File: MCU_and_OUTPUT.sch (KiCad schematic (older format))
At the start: 32 parts, among them P5 CONN_5, P6 CONN_01X04, Q2 BC817-40, Q3 BC817-40, Q4 BC807-40, Q5 IRF540, U2 STM32F030K6, U3 LM358

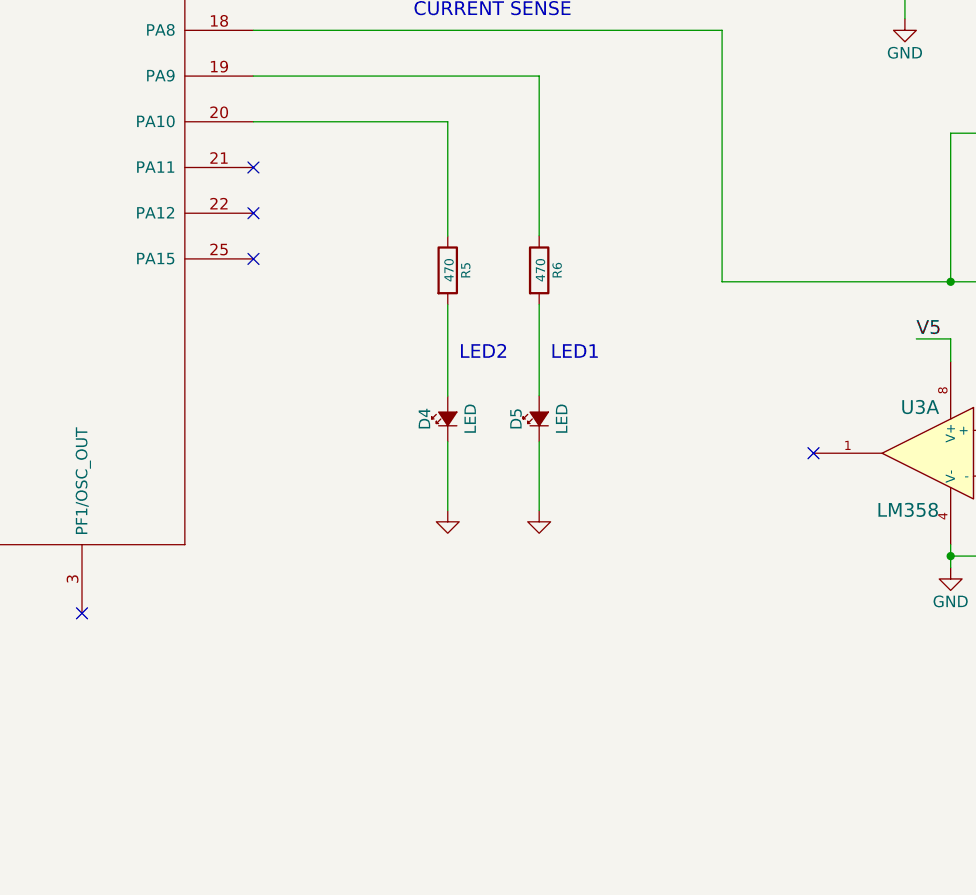
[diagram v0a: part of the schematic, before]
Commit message: agregue pulsador de arranque y buzzer
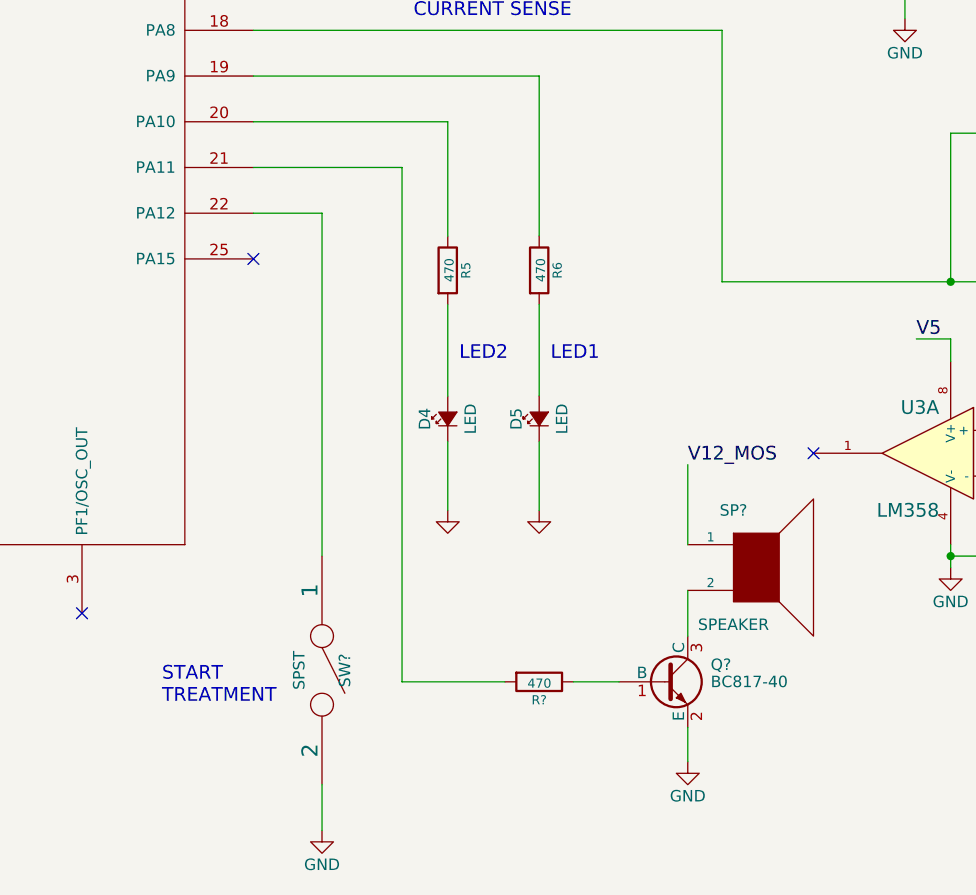
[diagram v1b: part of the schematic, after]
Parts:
- added Q?: BC817-40, MOSFET:BC817_SOT-23, symbol BC817-40
- added R?: 470, Resistors_SMD:R_0805_HandSoldering, symbol R
- added SP?: SPEAKER, symbol SPEAKER
- added SW?: SPST, symbol SPST
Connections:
- net GND: now also Q?.2 (E), SW?.2
- net V12_MOSFET: now also SP?.1
- net at U2.21 (PA11): now also R?.2
- net at U2.22 (PA12): now also SW?.1
- new net: Q?.1 (B), R?.1
- new net: Q?.3 (C), SP?.2
- no-connect marks 20 -> 18
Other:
- note added: "START\nTREATMENT"
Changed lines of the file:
@@
 	1    0    0    -1
 $EndComp
-NoConn ~ 4250 4800
 NoConn ~ 4250 5000
 NoConn ~ 1300 3200
@@
 $EndComp
 NoConn ~ 7550 6950
-NoConn ~ 4250 4600
 NoConn ~ 4250 2600
 Text HLabel 8300 800  2    60   Input ~ 0
@@
 Connection ~ 7300 6300
 NoConn ~ 6700 5850
+$Comp
+L GND #PWR?
+U 1 1 56FFF54C
+P 6150 7200
+F 0 "#PWR?" H 6150 6950 50  0001 C CNN
+F 1 "GND" H 6150 7050 50  0000 C CNN
+F 2 "" H 6150 7200 60  0000 C CNN
+F 3 "" H 6150 7200 60  0000 C CNN
+	1    6150 7200
+	1    0    0    -1
+$EndComp
+Text Label 6150 5900 0    60   ~ 0
+V12_MOS
+$Comp
+L BC817-40 Q?
+U 1 1 56FFF553
+P 6050 6850
+F 0 "Q?" H 6250 6925 50  0000 L CNN
+F 1 "BC817-40" H 6250 6850 50  0000 L CNN
+F 2 "MOSFET:BC817_SOT-23" H 6250 6775 50  0001 L CIN
+F 3 "" H 6050 6850 50  0000 L CNN
+	1    6050 6850
+	1    0    0    -1
+$EndComp
+Wire Wire Line
+	6150 6450 6150 6650
+Wire Wire Line
+	6150 7050 6150 7200
+Wire Wire Line
+	6150 5900 6150 6250
+$Comp
+L SPST SW?
+U 1 1 56FFFC2E
+P 4550 6800
+F 0 "SW?" H 4550 6900 50  0000 C CNN
+F 1 "SPST" H 4550 6700 50  0000 C CNN
+F 2 "" H 4550 6800 60  0000 C CNN
+F 3 "" H 4550 6800 60  0000 C CNN
+	1    4550 6800
+	0    1    1    0
+$EndComp
+$Comp
+L SPEAKER SP?
+U 1 1 56FFFCAD
+P 6450 6350
+F 0 "SP?" H 6350 6600 50  0000 C CNN
+F 1 "SPEAKER" H 6350 6100 50  0000 C CNN
+F 2 "" H 6450 6350 60  0000 C CNN
+F 3 "" H 6450 6350 60  0000 C CNN
+	1    6450 6350
+	1    0    0    -1
+$EndComp
+$Comp
+L GND #PWR?
+U 1 1 57000B38
+P 4550 7500
+F 0 "#PWR?" H 4550 7250 50  0001 C CNN
+F 1 "GND" H 4550 7350 50  0000 C CNN
+F 2 "" H 4550 7500 60  0000 C CNN
+F 3 "" H 4550 7500 60  0000 C CNN
+	1    4550 7500
+	1    0    0    -1
+$EndComp
+Wire Wire Line
+	4550 7300 4550 7500
+$Comp
+L R R?
+U 1 1 5700128D
+P 5500 6850
+F 0 "R?" V 5580 6850 40  0000 C CNN
+F 1 "470" V 5507 6851 40  0000 C CNN
+F 2 "Resistors_SMD:R_0805_HandSoldering" V 5430 6850 30  0001 C CNN
+F 3 "~" H 5500 6850 30  0000 C CNN
+	1    5500 6850
+	0    1    1    0
+$EndComp
+Wire Wire Line
+	4250 4600 4900 4600
+Wire Wire Line
+	4900 4600 4900 6850
+Wire Wire Line
+	4900 6850 5350 6850
+Wire Wire Line
+	5650 6850 5850 6850
+Wire Wire Line
+	4250 4800 4550 4800
+Wire Wire Line
+	4550 4800 4550 6300
+Text Notes 3850 6950 0    60   ~ 0
+START\nTREATMENT
 $EndSCHEMATC

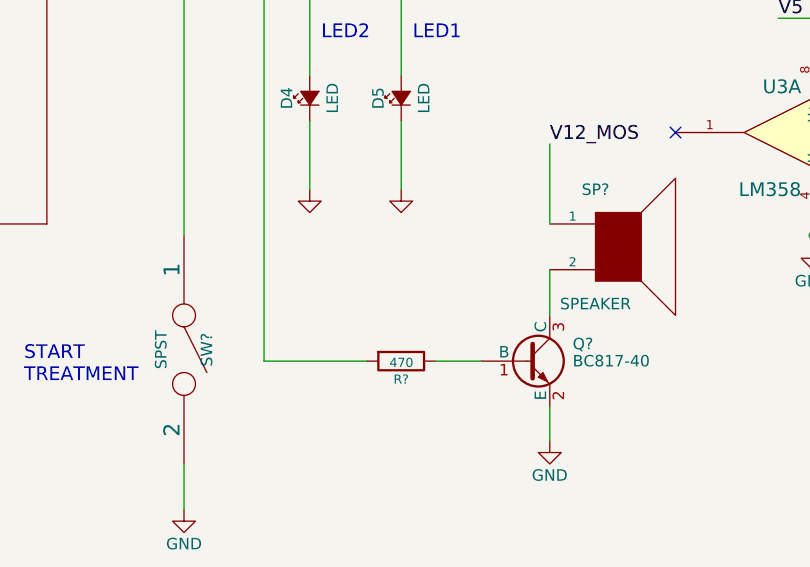
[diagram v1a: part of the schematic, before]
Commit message: agrego librerias de footprint y paso todo al PCB
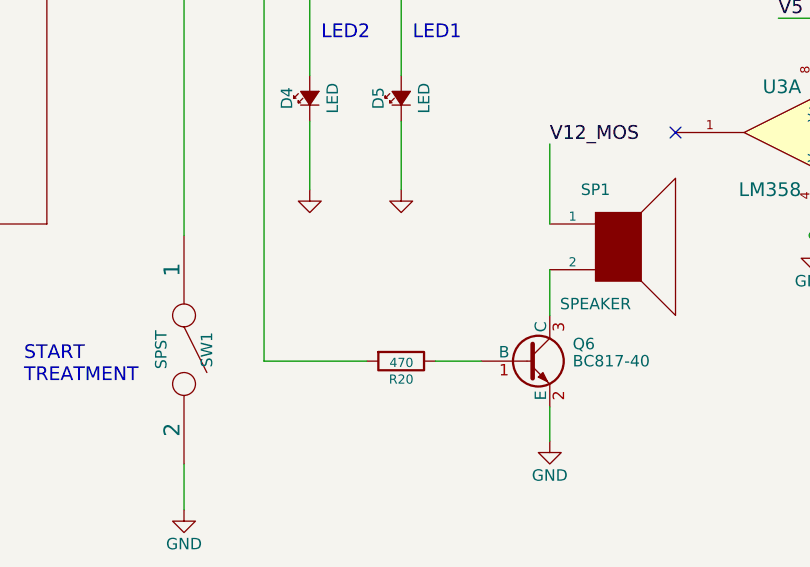
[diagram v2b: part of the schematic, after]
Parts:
- C8: footprint (none) -> LOCAL_Capacitors_ThroughHole:C_Radial_D5_L11_P2.5
- D6: footprint (none) -> LOCAL_Diode_ThroughHole:Diode_DO-41_SOD81_Horizontal_RM10
- D7: footprint Discret:D3 -> LOCAL_Diode_ThroughHole:Diode_DO-201AD_Horizontal_RM15
- D8: footprint (none) -> LOCAL_Diode_ThroughHole:Diode_DO-201AD_Horizontal_RM15
- P5: footprint Pin_Headers:Pin_Header_Straight_1x05 -> LOCAL_Pin_Headers:Pin_Header_Straight_1x05
- P6: footprint (none) -> LOCAL_Pin_Headers:Pin_Header_Straight_1x04
- Q2, Q3: footprint MOSFET:BC817_SOT-23 -> LOCAL_MOSFET:BC817_SOT-23
- Q4: footprint MOSFET:BC857_SOT-23 -> LOCAL_MOSFET:BC857_SOT-23
- Q5: footprint MOSFET:IRF540N_Vertical -> LOCAL_MOSFET:IRF540N_Vertical
- Q6: renamed from Q?; footprint MOSFET:BC817_SOT-23 -> LOCAL_MOSFET:BC817_SOT-23
- R13, R14, R15, R16: footprint (none) -> Resistors_SMD:R_0805_HandSoldering
- R18, R19: footprint (none) -> Resistors_ThroughHole:Resistor_Horizontal_RM20mm
- SP1: renamed from SP?; footprint (none) -> LOCAL_Pin_Headers:Pin_Header_Straight_1x02
- SW1: renamed from SW?; footprint (none) -> LOCAL_Pin_Headers:Pin_Header_Straight_1x02
- U3: footprint (none) -> Power_Integrations:SO-8
- gave numbers to parts that had none: 1
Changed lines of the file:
@@
 F 0 "P5" V 3050 950 50  0000 C CNN
 F 1 "CONN_5" V 3150 950 50  0000 C CNN
-F 2 "Pin_Headers:Pin_Header_Straight_1x05" H 3100 950 60  0001 C CNN
+F 2 "LOCAL_Pin_Headers:Pin_Header_Straight_1x05" H 3100 950 60  0001 C CNN
 F 3 "" H 3100 950 60  0000 C CNN
 	1    3100 950
@@
 F 0 "D7" H 9400 2750 50  0000 C CNN
 F 1 "SB520" H 9400 2550 50  0000 C CNN
-F 2 "Discret:D3" H 9400 2650 60  0001 C CNN
+F 2 "LOCAL_Diode_ThroughHole:Diode_DO-201AD_Horizontal_RM15" H 9400 2650 60  0001 C CNN
 F 3 "" H 9400 2650 60  0000 C CNN
 	1    9400 2650
@@
 F 0 "Q5" H 9560 3470 50  0000 R CNN
 F 1 "IRF540" H 9500 3150 50  0000 R CNN
-F 2 "MOSFET:IRF540N_Vertical" H 9550 3300 60  0001 C CNN
+F 2 "LOCAL_MOSFET:IRF540N_Vertical" H 9550 3300 60  0001 C CNN
 F 3 "" H 9550 3300 60  0000 C CNN
 	1    9550 3300
@@
 F 0 "Q3" H 8450 3125 50  0000 L CNN
 F 1 "BC817-40" H 8450 3050 50  0000 L CNN
-F 2 "MOSFET:BC817_SOT-23" H 8450 2975 50  0001 L CIN
+F 2 "LOCAL_MOSFET:BC817_SOT-23" H 8450 2975 50  0001 L CIN
 F 3 "" H 8250 3050 50  0000 L CNN
 	1    8250 3050
@@
 F 0 "Q2" H 7200 3675 50  0000 L CNN
 F 1 "BC817-40" H 7200 3600 50  0000 L CNN
-F 2 "MOSFET:BC817_SOT-23" H 7200 3525 50  0001 L CIN
+F 2 "LOCAL_MOSFET:BC817_SOT-23" H 7200 3525 50  0001 L CIN
 F 3 "" H 7000 3600 50  0000 L CNN
 	1    7000 3600
@@
 F 0 "Q4" H 8450 3675 50  0000 L CNN
 F 1 "BC807-40" H 8450 3600 50  0000 L CNN
-F 2 "MOSFET:BC857_SOT-23" H 8450 3525 50  0001 L CIN
+F 2 "LOCAL_MOSFET:BC857_SOT-23" H 8450 3525 50  0001 L CIN
 F 3 "" H 8250 3600 50  0000 L CNN
 	1    8250 3600
@@
 F 0 "U3" H 8000 5300 60  0000 L CNN
 F 1 "LM358" H 8000 4850 60  0000 L CNN
-F 2 "" H 8050 5100 60  0000 C CNN
+F 2 "Power_Integrations:SO-8" H 8050 5100 60  0001 C CNN
 F 3 "" H 8050 5100 60  0000 C CNN
 	2    8050 5100
@@
 F 0 "R19" V 9730 5350 50  0000 C CNN
 F 1 "0.33 2W" V 9650 5350 50  0000 C CNN
-F 2 "" V 9580 5350 30  0000 C CNN
+F 2 "Resistors_ThroughHole:Resistor_Horizontal_RM20mm" V 9580 5350 30  0001 C CNN
 F 3 "" H 9650 5350 30  0000 C CNN
 	1    9650 5350
@@
 F 0 "R18" V 9430 5350 50  0000 C CNN
 F 1 "0.33 2W" V 9350 5350 50  0000 C CNN
-F 2 "" V 9280 5350 30  0000 C CNN
+F 2 "Resistors_ThroughHole:Resistor_Horizontal_RM20mm" V 9280 5350 30  0001 C CNN
 F 3 "" H 9350 5350 30  0000 C CNN
 	1    9350 5350
@@
 F 0 "C8" H 8075 2500 50  0000 L CNN
 F 1 "10uF" H 8075 2300 50  0000 L CNN
-F 2 "" H 8050 2400 60  0000 C CNN
+F 2 "LOCAL_Capacitors_ThroughHole:C_Radial_D5_L11_P2.5" H 8050 2400 60  0001 C CNN
 F 3 "" H 8050 2400 60  0000 C CNN
 	1    8050 2400
@@
 F 0 "R13" V 8180 4450 50  0000 C CNN
 F 1 "100K" V 8100 4450 50  0000 C CNN
-F 2 "" V 8030 4450 30  0000 C CNN
+F 2 "Resistors_SMD:R_0805_HandSoldering" V 8030 4450 30  0001 C CNN
 F 3 "" H 8100 4450 30  0000 C CNN
 	1    8100 4450
@@
 F 0 "R16" V 8980 5200 50  0000 C CNN
 F 1 "10K" V 8900 5200 50  0000 C CNN
-F 2 "" V 8830 5200 30  0000 C CNN
+F 2 "Resistors_SMD:R_0805_HandSoldering" V 8830 5200 30  0001 C CNN
 F 3 "" H 8900 5200 30  0000 C CNN
 	1    8900 5200
@@
 F 0 "R15" V 8980 4450 50  0000 C CNN
 F 1 "10K" V 8900 4450 50  0000 C CNN
-F 2 "" V 8830 4450 30  0000 C CNN
+F 2 "Resistors_SMD:R_0805_HandSoldering" V 8830 4450 30  0001 C CNN
 F 3 "" H 8900 4450 30  0000 C CNN
 	1    8900 4450
@@
 F 0 "R14" V 8730 5550 50  0000 C CNN
 F 1 "100K" V 8650 5550 50  0000 C CNN
-F 2 "" V 8580 5550 30  0000 C CNN
+F 2 "Resistors_SMD:R_0805_HandSoldering" V 8580 5550 30  0001 C CNN
 F 3 "" H 8650 5550 30  0000 C CNN
 	1    8650 5550
@@
 F 0 "P6" H 10600 2100 50  0000 C CNN
 F 1 "CONN_01X04" V 10700 1850 50  0000 C CNN
-F 2 "" H 10600 1850 60  0000 C CNN
+F 2 "LOCAL_Pin_Headers:Pin_Header_Straight_1x04" H 10600 1850 60  0001 C CNN
 F 3 "" H 10600 1850 60  0000 C CNN
 	1    10600 1850
@@
 F 0 "D8" H 9650 2050 50  0000 C CNN
 F 1 "FR307" H 9650 1850 50  0000 C CNN
-F 2 "" H 9650 1950 60  0000 C CNN
+F 2 "LOCAL_Diode_ThroughHole:Diode_DO-201AD_Horizontal_RM15" H 9650 1950 60  0001 C CNN
 F 3 "" H 9650 1950 60  0000 C CNN
 	1    9650 1950
@@
 F 0 "D6" H 5700 2100 50  0000 C CNN
 F 1 "1n4007" H 5700 1900 50  0000 C CNN
-F 2 "" H 5700 2000 60  0000 C CNN
+F 2 "LOCAL_Diode_ThroughHole:Diode_DO-41_SOD81_Horizontal_RM10" H 5700 2000 60  0001 C CNN
 F 3 "" H 5700 2000 60  0000 C CNN
 	1    5700 2000
@@
 F 0 "U3" H 7150 6050 60  0000 L CNN
 F 1 "LM358" H 7150 5600 60  0000 L CNN
-F 2 "" H 7200 5850 60  0000 C CNN
+F 2 "Power_Integrations:SO-8" H 7200 5850 60  0001 C CNN
 F 3 "" H 7200 5850 60  0000 C CNN
 	1    7200 5850
@@
 NoConn ~ 6700 5850
 $Comp
-L GND #PWR?
+L GND #PWR030
 U 1 1 56FFF54C
 P 6150 7200
-F 0 "#PWR?" H 6150 6950 50  0001 C CNN
+F 0 "#PWR030" H 6150 6950 50  0001 C CNN
 F 1 "GND" H 6150 7050 50  0000 C CNN
 F 2 "" H 6150 7200 60  0000 C CNN
@@
 V12_MOS
 $Comp
-L BC817-40 Q?
+L BC817-40 Q6
 U 1 1 56FFF553
 P 6050 6850
-F 0 "Q?" H 6250 6925 50  0000 L CNN
+F 0 "Q6" H 6250 6925 50  0000 L CNN
 F 1 "BC817-40" H 6250 6850 50  0000 L CNN
-F 2 "MOSFET:BC817_SOT-23" H 6250 6775 50  0001 L CIN
+F 2 "LOCAL_MOSFET:BC817_SOT-23" H 6250 6775 50  0001 L CIN
 F 3 "" H 6050 6850 50  0000 L CNN
 	1    6050 6850
@@
 	6150 5900 6150 6250
 $Comp
-L SPST SW?
+L SPST SW1
 U 1 1 56FFFC2E
 P 4550 6800
-F 0 "SW?" H 4550 6900 50  0000 C CNN
+F 0 "SW1" H 4550 6900 50  0000 C CNN
 F 1 "SPST" H 4550 6700 50  0000 C CNN
-F 2 "" H 4550 6800 60  0000 C CNN
+F 2 "LOCAL_Pin_Headers:Pin_Header_Straight_1x02" H 4550 6800 60  0001 C CNN
 F 3 "" H 4550 6800 60  0000 C CNN
 	1    4550 6800
@@
 $EndComp
 $Comp
-L SPEAKER SP?
+L SPEAKER SP1
 U 1 1 56FFFCAD
 P 6450 6350
-F 0 "SP?" H 6350 6600 50  0000 C CNN
+F 0 "SP1" H 6350 6600 50  0000 C CNN
 F 1 "SPEAKER" H 6350 6100 50  0000 C CNN
-F 2 "" H 6450 6350 60  0000 C CNN
+F 2 "LOCAL_Pin_Headers:Pin_Header_Straight_1x02" H 6450 6350 60  0001 C CNN
 F 3 "" H 6450 6350 60  0000 C CNN
 	1    6450 6350
@@
 $EndComp
 $Comp
-L GND #PWR?
+L GND #PWR031
 U 1 1 57000B38
 P 4550 7500
-F 0 "#PWR?" H 4550 7250 50  0001 C CNN
+F 0 "#PWR031" H 4550 7250 50  0001 C CNN
 F 1 "GND" H 4550 7350 50  0000 C CNN
 F 2 "" H 4550 7500 60  0000 C CNN
@@
 	4550 7300 4550 7500
 $Comp
-L R R?
+L R R20
 U 1 1 5700128D
 P 5500 6850
-F 0 "R?" V 5580 6850 40  0000 C CNN
+F 0 "R20" V 5580 6850 40  0000 C CNN
 F 1 "470" V 5507 6851 40  0000 C CNN
 F 2 "Resistors_SMD:R_0805_HandSoldering" V 5430 6850 30  0001 C CNN

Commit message: mas pistas pero sin micro
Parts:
- SP1: footprint LOCAL_Pin_Headers:Pin_Header_Straight_1x02 -> LOCAL_Capacitors_ThroughHole:C_Radial_D10_L20_P5
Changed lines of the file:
@@
 F 0 "SP1" H 6350 6600 50  0000 C CNN
 F 1 "SPEAKER" H 6350 6100 50  0000 C CNN
-F 2 "LOCAL_Pin_Headers:Pin_Header_Straight_1x02" H 6450 6350 60  0001 C CNN
+F 2 "LOCAL_Capacitors_ThroughHole:C_Radial_D10_L20_P5" H 6450 6350 60  0001 C CNN
 F 3 "" H 6450 6350 60  0000 C CNN
 	1    6450 6350

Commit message: mas routeado casi terminado
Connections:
- net at U2.19 (PA9): no longer R6.1
- net at U2.20 (PA10): no longer R5.1
- net at U2.21 (PA11): no longer R20.2
- net at U2.22 (PA12): no longer SW1.1
- net at U2.26 (PB3): now also R5.1
- net at U2.28 (PB5): now also R6.1
- net at U2.30 (PB7): now also SW1.1
- net at U2.8 (PA2): now also R20.2
- no-connect marks 18 -> 17
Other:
- moved on the sheet: D4, D5, R5, R6, SW1
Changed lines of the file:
@@
 L R R5
 U 1 1 56FC59AC
-P 5100 5050
-F 0 "R5" V 5180 5050 40  0000 C CNN
-F 1 "470" V 5107 5051 40  0000 C CNN
-F 2 "Resistors_SMD:R_0805_HandSoldering" V 5030 5050 30  0001 C CNN
-F 3 "~" H 5100 5050 30  0000 C CNN
-	1    5100 5050
+P 650 3850
+F 0 "R5" V 730 3850 40  0000 C CNN
+F 1 "470" V 657 3851 40  0000 C CNN
+F 2 "Resistors_SMD:R_0805_HandSoldering" V 580 3850 30  0001 C CNN
+F 3 "~" H 650 3850 30  0000 C CNN
+	1    650  3850
 	1    0    0    -1
 $EndComp
@@
 L Led_Small D4
 U 1 1 56FC59AD
-P 5100 5700
-F 0 "D4" H 5100 5800 50  0000 C CNN
-F 1 "LED" H 5100 5600 50  0000 C CNN
-F 2 "LEDs:LED-3MM" H 5100 5700 60  0001 C CNN
-F 3 "~" H 5100 5700 60  0000 C CNN
-	1    5100 5700
+P 650 4500
+F 0 "D4" H 650 4600 50  0000 C CNN
+F 1 "LED" H 650 4400 50  0000 C CNN
+F 2 "LEDs:LED-3MM" H 650 4500 60  0001 C CNN
+F 3 "~" H 650 4500 60  0000 C CNN
+	1    650  4500
 	0    -1   -1   0
 $EndComp
@@
 L GND #PWR016
 U 1 1 56FC59AE
-P 5100 6100
-F 0 "#PWR016" H 5100 6100 30  0001 C CNN
-F 1 "GND" H 5100 6030 30  0001 C CNN
-F 2 "" H 5100 6100 60  0000 C CNN
-F 3 "" H 5100 6100 60  0000 C CNN
-	1    5100 6100
+P 650 4900
+F 0 "#PWR016" H 650 4900 30  0001 C CNN
+F 1 "GND" H 650 4830 30  0001 C CNN
+F 2 "" H 650 4900 60  0000 C CNN
+F 3 "" H 650 4900 60  0000 C CNN
+	1    650  4900
 	1    0    0    -1
 $EndComp
@@
 $EndComp
 NoConn ~ 4250 5000
-NoConn ~ 1300 3200
-NoConn ~ 1300 3800
-NoConn ~ 1300 3400
-NoConn ~ 1300 3600
 $Comp
 L R R4
@@
 NoConn ~ 1300 2800
 NoConn ~ 1300 3000
-NoConn ~ 1300 4000
 NoConn ~ 4250 3800
-NoConn ~ 4250 2800
 NoConn ~ 4250 3000
 NoConn ~ 4250 3200
@@
 L R R6
 U 1 1 56FC59B2
-P 5500 5050
-F 0 "R6" V 5580 5050 40  0000 C CNN
-F 1 "470" V 5507 5051 40  0000 C CNN
-F 2 "Resistors_SMD:R_0805_HandSoldering" V 5430 5050 30  0001 C CNN
-F 3 "~" H 5500 5050 30  0000 C CNN
-	1    5500 5050
+P 850 4700
+F 0 "R6" V 930 4700 40  0000 C CNN
+F 1 "470" V 857 4701 40  0000 C CNN
+F 2 "Resistors_SMD:R_0805_HandSoldering" V 780 4700 30  0001 C CNN
+F 3 "~" H 850 4700 30  0000 C CNN
+	1    850  4700
 	1    0    0    -1
 $EndComp
@@
 L Led_Small D5
 U 1 1 56FC59B3
-P 5500 5700
-F 0 "D5" H 5500 5800 50  0000 C CNN
-F 1 "LED" H 5500 5600 50  0000 C CNN
-F 2 "LEDs:LED-3MM" H 5500 5700 60  0001 C CNN
-F 3 "~" H 5500 5700 60  0000 C CNN
-	1    5500 5700
+P 850 5350
+F 0 "D5" H 850 5450 50  0000 C CNN
+F 1 "LED" H 850 5250 50  0000 C CNN
+F 2 "LEDs:LED-3MM" H 850 5350 60  0001 C CNN
+F 3 "~" H 850 5350 60  0000 C CNN
+	1    850  5350
 	0    -1   -1   0
 $EndComp
@@
 L GND #PWR018
 U 1 1 56FC59B4
-P 5500 6100
-F 0 "#PWR018" H 5500 6100 30  0001 C CNN
-F 1 "GND" H 5500 6030 30  0001 C CNN
-F 2 "" H 5500 6100 60  0000 C CNN
-F 3 "" H 5500 6100 60  0000 C CNN
-	1    5500 6100
+P 850 5750
+F 0 "#PWR018" H 850 5750 30  0001 C CNN
+F 1 "GND" H 850 5680 30  0001 C CNN
+F 2 "" H 850 5750 60  0000 C CNN
+F 3 "" H 850 5750 60  0000 C CNN
+	1    850  5750
 	1    0    0    -1
 $EndComp
@@
 Text Label 7600 1300 0    60   ~ 0
 V3.3_ANALOG
-Text Notes 5550 5450 0    60   ~ 0
+Text Notes 900  5100 0    60   ~ 0
 LED1
-Text Notes 5150 5450 0    60   ~ 0
+Text Notes 700  4250 0    60   ~ 0
 LED2
 $Comp
@@
 Connection ~ 1900 1500
 Wire Wire Line
-	5100 5800 5100 6100
-Wire Wire Line
-	5100 5200 5100 5600
+	650  4600 650  4900
+Wire Wire Line
+	650  4000 650  4400
 Connection ~ 2050 1500
 Wire Wire Line
@@
 	7600 1050 8300 1050
 Wire Wire Line
-	5500 5800 5500 6100
-Wire Wire Line
-	5500 5200 5500 5600
-Wire Wire Line
-	5500 4200 5500 4900
-Wire Wire Line
-	5500 4200 4250 4200
-Wire Wire Line
-	4250 4400 5100 4400
-Wire Wire Line
-	5100 4400 5100 4900
+	850  5450 850  5750
+Wire Wire Line
+	850  4850 850  5250
 Wire Wire Line
 	7600 1300 8300 1300
@@
 Wire Wire Line
 	5000 2400 4250 2400
-$Comp
-L STM32F030K6 U2
-U 1 1 56FC59A8
-P 2800 4250
-F 0 "U2" H 3800 6700 40  0000 C CNN
-F 1 "STM32F030K6" H 2800 4250 40  0000 C CNN
-F 2 "Housings_QFP:TQFP-32_7x7mm_Pitch0.8mm" H 2850 3900 30  0001 C CIN
-F 3 "" H 2850 3900 60  0000 C CNN
-	1    2800 4250
-	1    0    0    -1
-$EndComp
 Text Notes 4450 2350 0    60   ~ 0
 SYNC SIGNAL
@@
 L SPST SW1
 U 1 1 56FFFC2E
-P 4550 6800
-F 0 "SW1" H 4550 6900 50  0000 C CNN
-F 1 "SPST" H 4550 6700 50  0000 C CNN
-F 2 "LOCAL_Pin_Headers:Pin_Header_Straight_1x02" H 4550 6800 60  0001 C CNN
-F 3 "" H 4550 6800 60  0000 C CNN
-	1    4550 6800
+P 1200 6600
+F 0 "SW1" H 1200 6700 50  0000 C CNN
+F 1 "SPST" H 1200 6500 50  0000 C CNN
+F 2 "LOCAL_Pin_Headers:Pin_Header_Straight_1x02" H 1200 6600 60  0001 C CNN
+F 3 "" H 1200 6600 60  0000 C CNN
+	1    1200 6600
 	0    1    1    0
 $EndComp
@@
 L GND #PWR031
 U 1 1 57000B38
-P 4550 7500
-F 0 "#PWR031" H 4550 7250 50  0001 C CNN
-F 1 "GND" H 4550 7350 50  0000 C CNN
-F 2 "" H 4550 7500 60  0000 C CNN
-F 3 "" H 4550 7500 60  0000 C CNN
-	1    4550 7500
-	1    0    0    -1
-$EndComp
-Wire Wire Line
-	4550 7300 4550 7500
+P 1200 7300
+F 0 "#PWR031" H 1200 7050 50  0001 C CNN
+F 1 "GND" H 1200 7150 50  0000 C CNN
+F 2 "" H 1200 7300 60  0000 C CNN
+F 3 "" H 1200 7300 60  0000 C CNN
+	1    1200 7300
+	1    0    0    -1
+$EndComp
 $Comp
 L R R20
@@
 $EndComp
 Wire Wire Line
-	4250 4600 4900 4600
-Wire Wire Line
-	4900 4600 4900 6850
+	4900 2800 4900 6850
 Wire Wire Line
 	4900 6850 5350 6850
 Wire Wire Line
 	5650 6850 5850 6850
-Wire Wire Line
-	4250 4800 4550 4800
-Wire Wire Line
-	4550 4800 4550 6300
-Text Notes 3850 6950 0    60   ~ 0
+Text Notes 550  6800 0    60   ~ 0
 START\nTREATMENT
+NoConn ~ 4250 4200
+NoConn ~ 4250 4400
+$Comp
+L STM32F030K6 U2
+U 1 1 56FC59A8
+P 2800 4250
+F 0 "U2" H 3800 6700 40  0000 C CNN
+F 1 "STM32F030K6" H 2800 4250 40  0000 C CNN
+F 2 "Housings_QFP:TQFP-32_7x7mm_Pitch0.8mm" H 2850 3900 30  0001 C CIN
+F 3 "" H 2850 3900 60  0000 C CNN
+	1    2800 4250
+	1    0    0    -1
+$EndComp
+NoConn ~ 4250 4800
+Wire Wire Line
+	1300 4000 1200 4000
+Wire Wire Line
+	1200 4000 1200 6100
+Wire Wire Line
+	1200 7100 1200 7300
+Wire Wire Line
+	1300 3600 850  3600
+Wire Wire Line
+	850  3600 850  4550
+Wire Wire Line
+	1300 3200 650  3200
+Wire Wire Line
+	650  3200 650  3700
+NoConn ~ 1300 3400
+NoConn ~ 1300 3800
+Wire Wire Line
+	4900 2800 4250 2800
 $EndSCHEMATC
